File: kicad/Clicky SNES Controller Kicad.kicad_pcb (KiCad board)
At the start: 2 copper layers, 41.9 x 44.8 mm, 49 parts, among them P1 CN1, P10 SHIFT_PORT_ABXY, P11 TL_LINK_ABXY, P12 YB_LINK_ABXY, P13 TR_LINK_ABXY, P2 VSS_LINK_Trigger, P3 TR_TL_LINK_Trigger, P4 SelStart_LINK_DPAD, P5 YB_LINK_DPAD, P6 SHIFT_PORT_DPAD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

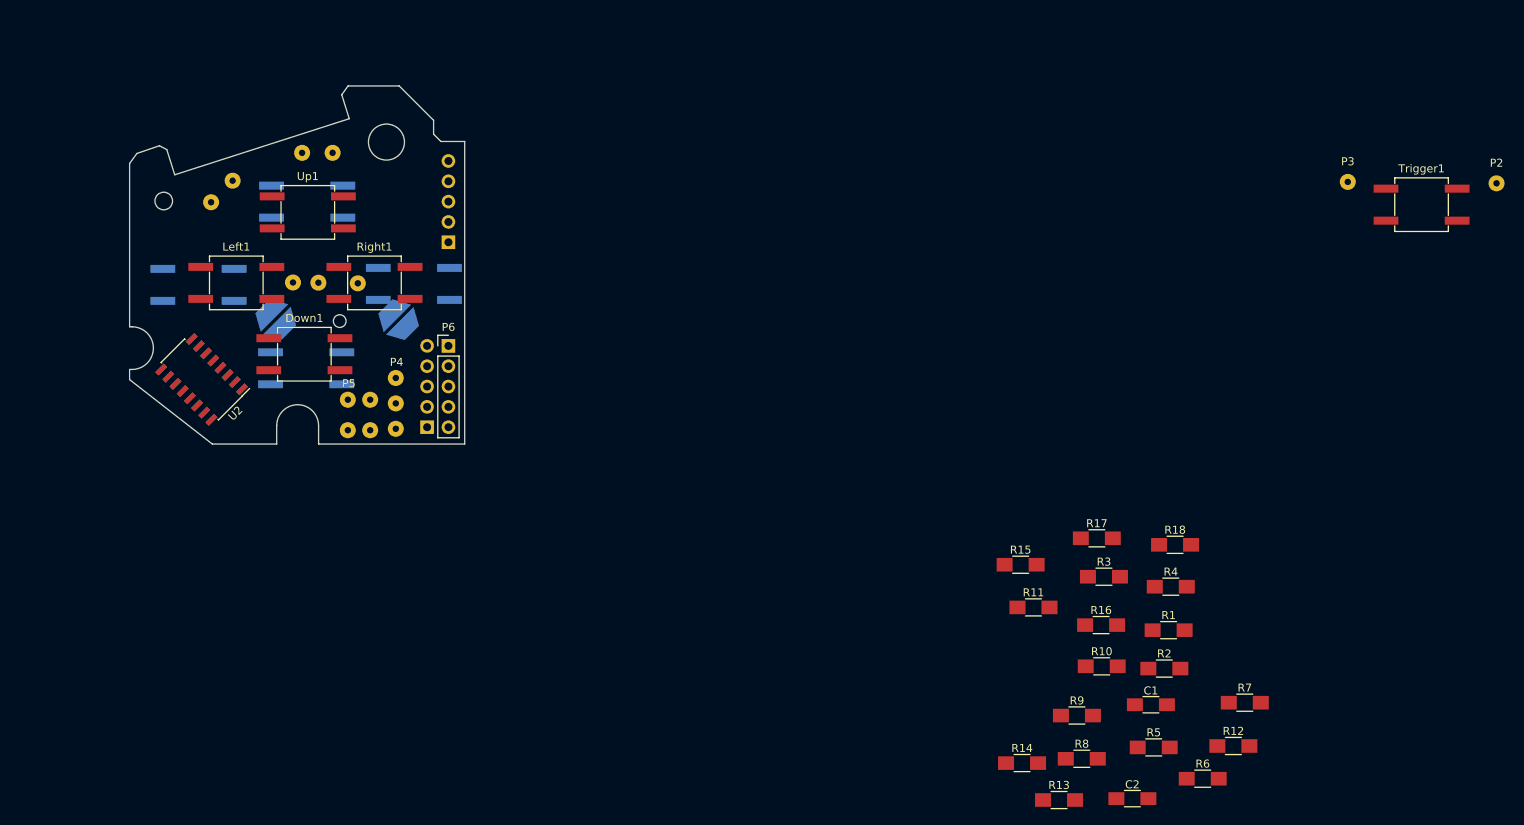
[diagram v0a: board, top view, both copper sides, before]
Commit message: PCB Rev 3: Import updated netlist
Many components removed/updated so complex netlist import.
Had to lock some manually placed pads (mounting holes).
Added some additional keep-out regions for the main board:
 - There is cross on the top side of the main board
 - There is a ring behind the select/start buttons on the main board
 - I put these keep-outs on the Cmts.User layer
Removed unnecessary 45 degree rotations from various components.
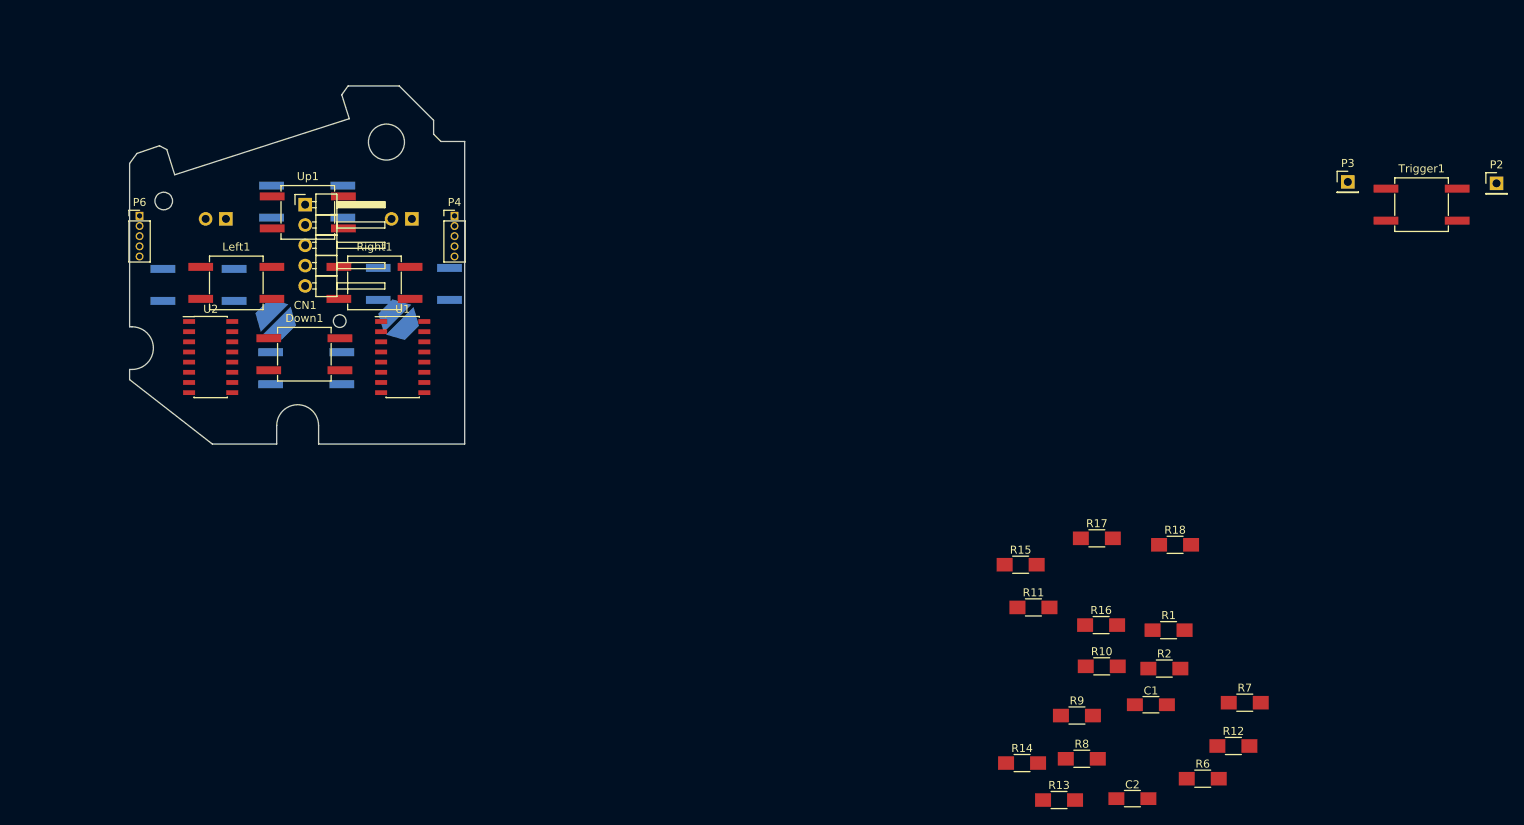
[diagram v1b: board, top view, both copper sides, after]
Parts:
- removed P10: SHIFT_PORT_ABXY, Pin_Headers:Pin_Header_Straight_1x05_Pitch2.54mm
- removed P12: YB_LINK_ABXY, Wire_Pads:SolderWirePad_2x_0-8mmDrill
- removed P5: YB_LINK_DPAD, Wire_Pads:SolderWirePad_2x_0-8mmDrill
- removed P7: VSS_LINK_SelStart, Wire_Pads:SolderWirePad_single_0-8mmDrill
- removed P8: Select_LINK_SelStart, Wire_Pads:SolderWirePad_single_0-8mmDrill
- removed P9: Start_LINK_SelStart, Wire_Pads:SolderWirePad_single_0-8mmDrill
- removed R3, R4, R5: 47k, Resistors_SMD:R_1206_HandSoldering
- CN1: renamed from P1; moved to F.Cu
- P11: value TL_LINK_ABXY -> TL_IN; footprint Wire_Pads:SolderWirePad_2x_0-8mmDrill -> Pin_Headers:Pin_Header_Angled_1x02_Pitch2.54mm
- P13: value TR_LINK_ABXY -> TR_IN; footprint Wire_Pads:SolderWirePad_2x_0-8mmDrill -> Pin_Headers:Pin_Header_Angled_1x02_Pitch2.54mm
- P2: value VSS_LINK_Trigger -> VSS_Trigger; footprint Wire_Pads:SolderWirePad_single_0-8mmDrill -> Pin_Headers:Pin_Header_Straight_1x01_Pitch2.54mm
- P3: value TR_TL_LINK_Trigger -> TR_TL_OUT; footprint Wire_Pads:SolderWirePad_single_0-8mmDrill -> Pin_Headers:Pin_Header_Straight_1x01_Pitch2.54mm
- P4: value SelStart_LINK_DPAD -> DPAD_IN; footprint Wire_Pads:SolderWirePad_3x_0-8mmDrill -> Pin_Headers:Pin_Header_Straight_1x05_Pitch1.27mm
- P6: value SHIFT_PORT_DPAD -> ABXY_IN; footprint Pin_Headers:Pin_Header_Straight_1x05_Pitch2.54mm -> Pin_Headers:Pin_Header_Straight_1x05_Pitch1.27mm
- U1: value 4021_DPAD -> 4021; moved to F.Cu
- U2: value 4021_ABXY -> 4021
- moved P6 41.9 mm to (14.0, 29.2)
- moved U1 25.3 mm to (46.9, 46.9), turned to 0 degrees
- moved P4 24.6 mm to (53.3, 29.2), turned to 0 degrees
- moved CN1 18.5 mm to (34.7, 27.8)
- moved P11 14.4 mm to (48.0, 29.6), turned to 90 degrees
- moved P13 3.47 mm to (24.8, 29.6), turned to 90 degrees
- moved U2 3.02 mm to (22.9, 46.9), turned to 0 degrees
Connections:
- A1 pad 1: VSS_ABXY -> GND
- A1 pad 2: /A -> /A_switch
- B1 pad 1: VSS_ABXY -> GND
- B1 pad 2: /B_LINK -> /B_switch
- C2 pad 1: VDD_ABXY -> +5V
- C2 pad 2: VSS_ABXY -> GND
- CN1 pad 2: /CLK_DPAD -> /DCLK
- Down1 pad 2: /Down -> /B_switch
- P11 pad 1: /TL -> GND
- P13 pad 1: /TR -> GND
- P4 pad 1: /Start -> GND
- P6 pad 1: +5V -> GND
- P6 pad 2: /CLK_DPAD -> /A
- P6 pad 3: /DLATCH -> /B
- P6 pad 4: /SERIN_DPAD -> /X
- P6 pad 5: GND -> /Y
- R1 pad 1: /CLK_DPAD -> /DCLK
- R10 pad 2: VDD_ABXY -> +5V
- R13 pad 1: /Down -> /B_switch
- R14 pad 1: /Up -> /A_switch
- R6 pad 2: VDD_ABXY -> +5V
- R7 pad 2: VDD_ABXY -> +5V
- R8 pad 2: VDD_ABXY -> +5V
- R9 pad 2: VDD_ABXY -> +5V
- Select1 pad 1: /VSS_SelStart -> GND
- Select1 pad 2: /Select_LINK -> /Select
- Start1 pad 1: /VSS_SelStart -> GND
- Start1 pad 2: /Start_LINK -> /Start
- U1 pad 10: /CLK_DPAD -> /DCLK
- U1 pad 11: /SERIN_DPAD -> Net-(U1-Pad11)
- U1 pad 4: /Up -> /A_switch
- U1 pad 5: /Down -> /B_switch
- U2 pad 10: /CLK_ABXY -> /DCLK
- U2 pad 11: VDD_ABXY -> +5V
- U2 pad 16: VDD_ABXY -> +5V
- U2 pad 3: /SEROUT_ABXY -> Net-(U1-Pad11)
- U2 pad 5: Net-(R5-Pad1) -> +5V
- U2 pad 6: Net-(R4-Pad1) -> +5V
- U2 pad 7: Net-(R3-Pad1) -> +5V
- U2 pad 8: VSS_ABXY -> GND
- U2 pad 9: /LATCH_ABXY -> /DLATCH
- Up1 pad 2: /Up -> /A_switch
- X1 pad 1: VSS_ABXY -> GND
- X1 pad 2: /X -> /Left
- Y1 pad 1: VSS_ABXY -> GND
- Y1 pad 2: /Y_LINK -> /Right

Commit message: SCH/NET: Remove extra pullup, Rename CN1 PCB: Imported new netlist, Arranged resistors in order
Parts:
- removed R6: 47k, Resistors_SMD:R_1206_HandSoldering
- R1, R2: moved to B.Cu
- moved R12 169.5 mm to (1.52, 15.0)
- moved R7 157.4 mm to (1.52, 44.2)
- moved R13 152.8 mm to (1.52, 17.8)
- moved R18 147.0 mm to (1.52, 31.8)
- moved R14 144.9 mm to (1.52, 20.6)
- moved R16 143.3 mm to (1.52, 26.2)
- moved R11 140.6 mm to (1.52, 12.2)
- moved R8 139.5 mm to (1.52, 47.0)
- moved R17 138.2 mm to (1.52, 29.0)
- moved R10 136.7 mm to (1.52, 52.6)
- moved R9 136.2 mm to (1.52, 49.8)
- moved R1 133.5 mm to (32.8, 5.08)
- moved C2 132.6 mm to (17.5, 46.7), turned to 270 degrees
- moved R15 132.2 mm to (1.52, 23.4)
- moved R2 129.4 mm to (40.9, 5.08)
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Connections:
- U2 pad 4: Net-(R6-Pad1) -> +5V

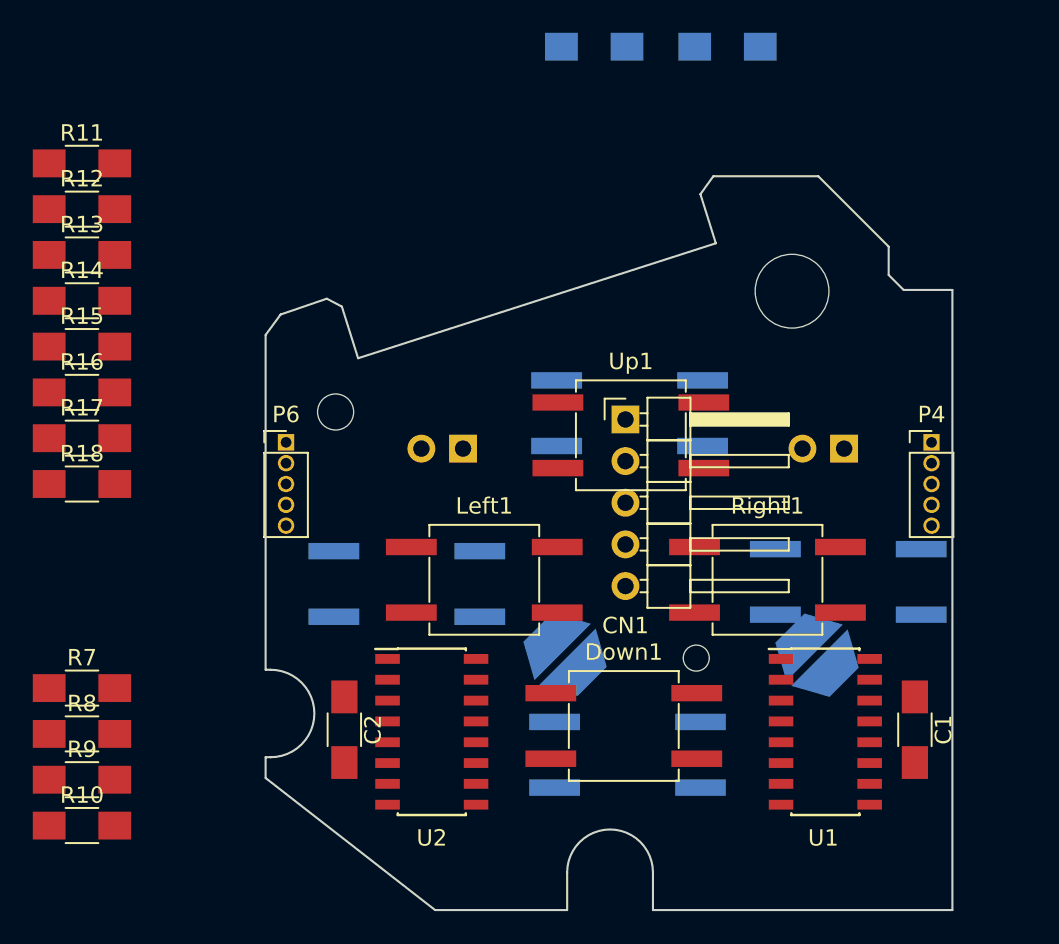
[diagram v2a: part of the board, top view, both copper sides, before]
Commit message: PCB: Place passive components
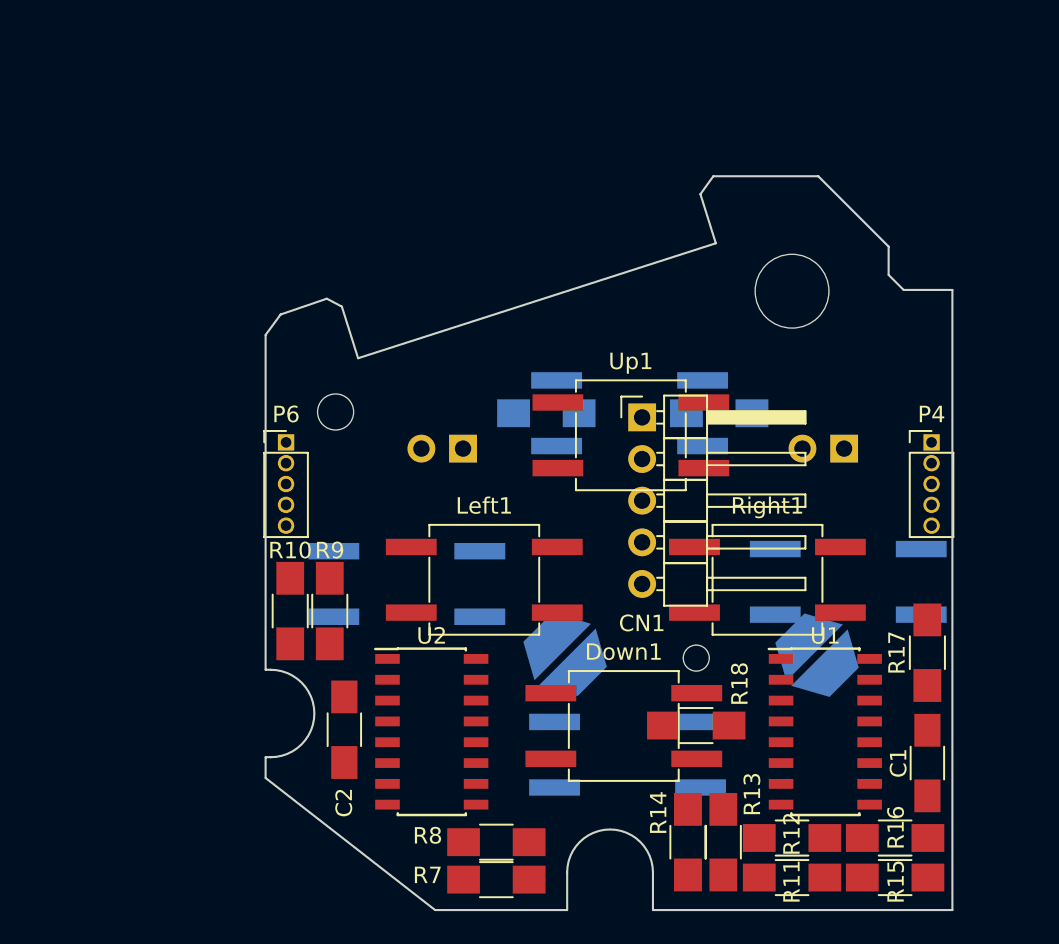
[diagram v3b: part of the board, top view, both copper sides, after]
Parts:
- moved R11 61.4 mm to (44.8, 55.8), turned to 180 degrees
- moved R15 59.2 mm to (51.1, 55.8)
- moved R12 57.8 mm to (44.8, 53.3), turned to 180 degrees
- moved R16 56.6 mm to (51.1, 53.3)
- moved R17 53.2 mm to (53.1, 42.0), turned to 90 degrees
- moved R13 53.0 mm to (40.6, 53.6), turned to 270 degrees
- moved R14 49.6 mm to (38.5, 53.6), turned to 270 degrees
- moved R18 40.3 mm to (39.0, 46.5), turned to 180 degrees
- moved R7 27.8 mm to (26.8, 55.9), turned to 180 degrees
- moved R8 26.1 mm to (26.8, 53.6), turned to 180 degrees
- moved R1 22.5 mm to (29.8, 27.4)
- moved R2 22.4 mm to (40.4, 27.4), turned to 180 degrees
- moved R9 18.3 mm to (16.6, 39.5), turned to 270 degrees
- moved R10 18.2 mm to (14.2, 39.5), turned to 270 degrees
- moved C1 2.17 mm to (53.1, 48.8), turned to 90 degrees
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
